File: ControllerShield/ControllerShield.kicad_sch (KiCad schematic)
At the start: 7 parts, among them J1 Power, J2 Digital/PWM, J3 Analog, J4 Digital/PWM, U1 COM-09032, U2 LIS3DH, U3 LSF0102DQER

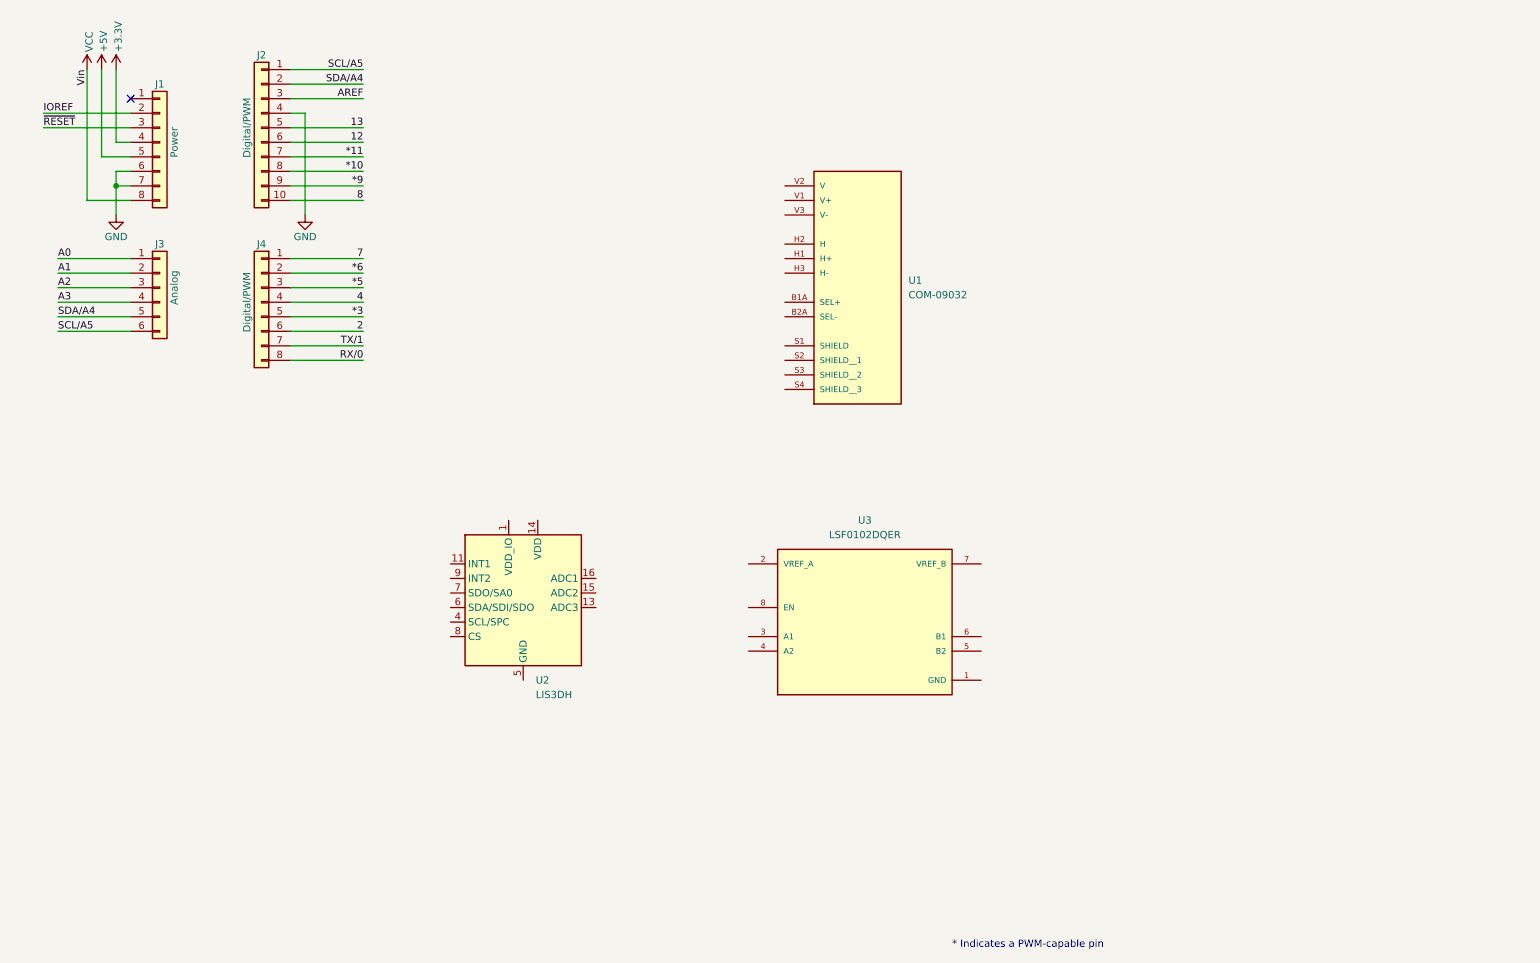
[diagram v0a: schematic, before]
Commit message: Tweak the connector board a bit.  Rearrange X and Y.  May do more depending on the other board.
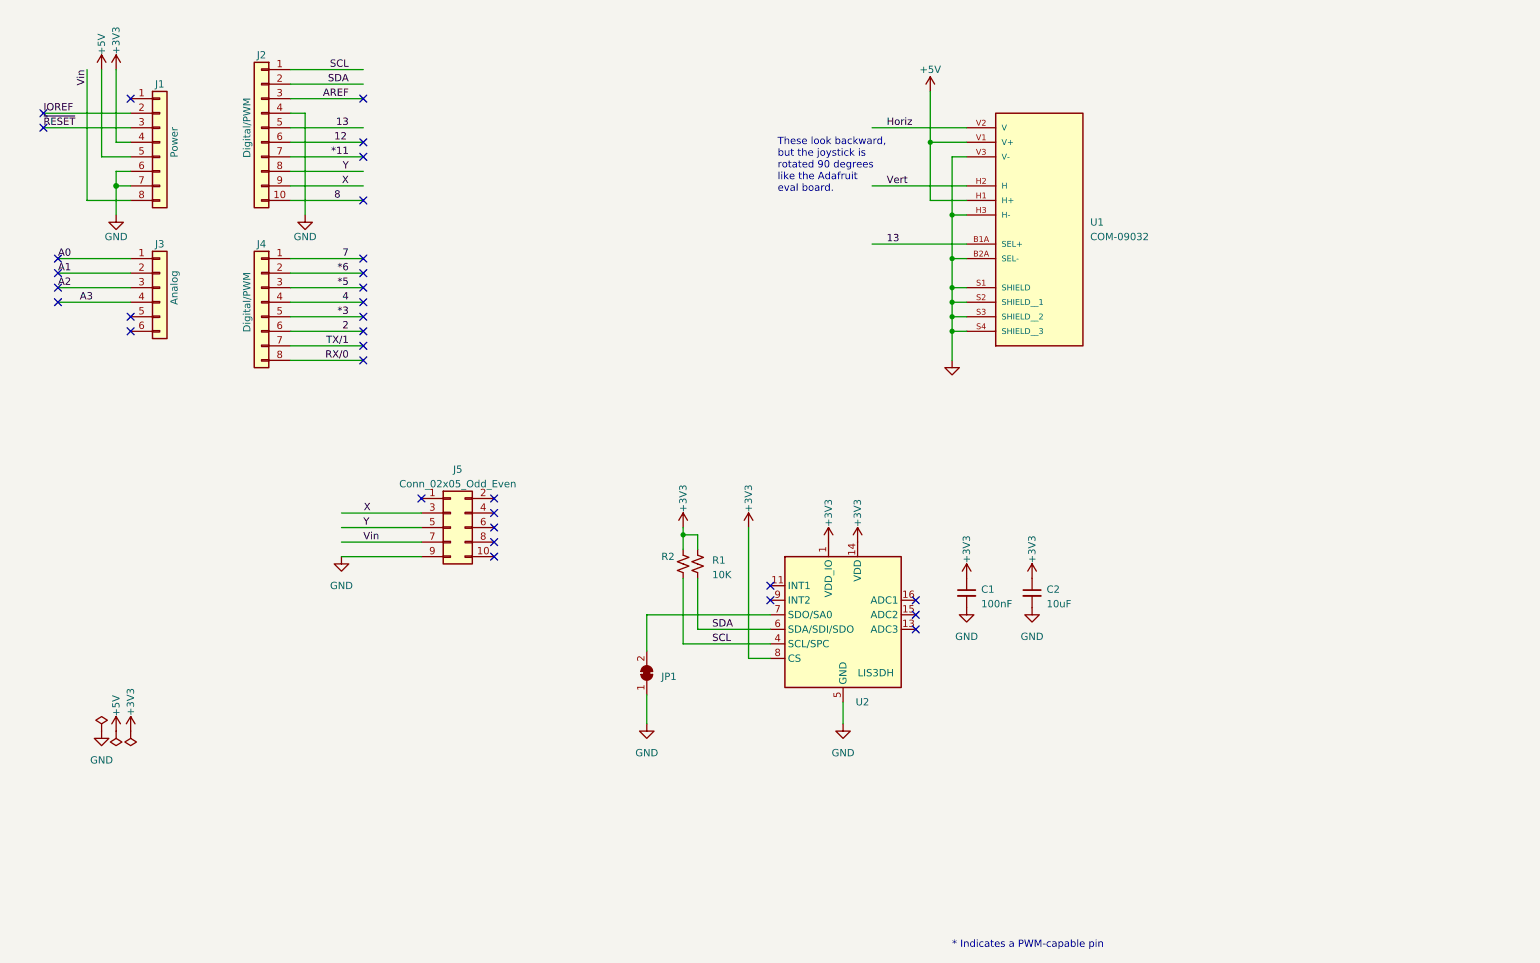
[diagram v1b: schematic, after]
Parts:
- removed U3: LSF0102DQER, Footprints:SON35P140X100X40-8N, symbol Local:LSF0102DQER
- added C1: 100nF, Capacitor_SMD:C_0603_1608Metric, symbol Device:C_Small
- added C2: 10uF, Capacitor_SMD:C_0603_1608Metric, symbol Device:C_Small
- added J5: Conn_02x05_Odd_Even, Connector_PinHeader_2.54mm:PinHeader_2x05_P2.54mm_Vertical, symbol Connector_Generic:Conn_02x05_Odd_Even
- added JP1: SolderJumper_2_Bridged, Jumper:SolderJumper-2_P1.3mm_Bridged_RoundedPad1.0x1.5mm, symbol Jumper:SolderJumper_2_Bridged
- added R1, R2: 10K, Resistor_SMD:R_0603_1608Metric, symbol Device:R_Small_US
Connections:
- net +3V3: now also U2.1 (VDD_IO), U2.14 (VDD), U2.8 (CS), C1.1, C2.1, R1.1, R2.1
- net +5V: now also U1.H1 (H+), U1.V1 (V+)
- net 13: now also U1.B1A (SEL+)
- net GND: now also U1.B2A (SEL-), U1.H3 (H-), U1.S1 (SHIELD), U1.S2 (SHIELD__1), U1.S3 (SHIELD__2), U1.S4 (SHIELD__3), U1.V3 (V-), U2.10 (GND), U2.12 (GND), U2.5 (GND), C1.2, C2.2, J5.9 (Pin_9), JP1.1 (A)
- net Vert: now reaches U1.H2 (H)
- net Horiz: now reaches U1.V2 (V)
- net SCL: now reaches U2.4 (SCL/SPC)
- net SCL: now also J2.1 (Pin_1), R2.2
- net SDA: now reaches U2.6 (SDA/SDI/SDO)
- net SDA: now also J2.2 (Pin_2), R1.2
- net at U2.7 (SDO/SA0): now also JP1.2 (B)
- net *10 renamed Y
- net Y: now also J5.5 (Pin_5)
- net *9 renamed X
- net X: now also J5.3 (Pin_3)
- net SCL/A5: no longer names the net of J3.6 (Pin_6)
- net SCL/A5: no longer J2.1 (Pin_1)
- net SDA/A4: no longer names the net of J3.5 (Pin_5)
- net SDA/A4: no longer J2.2 (Pin_2)
- net VCC renamed Vin
- net Vin: now also J5.7 (Pin_7)
- no-connect marks 1 -> 32
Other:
- note added: "These look backward, but the joystick is rotated 90 degrees like the Adafruit eval board."
- moved on the sheet: U1, U2

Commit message: Not sure what changes, but it was minor...
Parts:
- added D1: RED, symbol Device:LED
- added D2: Green, symbol Device:LED
- added R3, R4: 1K, symbol Device:R_Small_US
- C1: value 100nF -> 0.1uF
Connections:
- net 12 is gone; now on net D1: J2.6 (Pin_6)
- net A0 is gone; now on net Horiz: J3.1 (Pin_1)
- net A1 is gone; now on net Vert: J3.2 (Pin_2)
- net GND: now also D1.1 (K), D2.1 (K)
- net SCL: now also J5.3 (Pin_3)
- net SDA: now also J5.4 (Pin_4)
- net X: now also J5.1 (Pin_1); no longer J5.3 (Pin_3)
- net Y: now also J5.2 (Pin_2); no longer J5.5 (Pin_5)
- net D1: now reaches J5.6 (Pin_6)
- net *3 renamed Red
- net Red: now also R3.1
- net 13 renamed D0
- net D0: now also J5.5 (Pin_5); no longer U1.B1A (SEL+)
- net 2 renamed GameBtn
- net GameBtn: now also U1.B1A (SEL+)
- net 4 renamed Green
- net Green: now also R4.1
- net Vin renamed Vsys
- new net: D2.2 (A), R4.2
- new net: D1.2 (A), R3.2
- no-connect marks 32 -> 22

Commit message: work on controller
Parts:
- D1, D2: footprint (none) -> Diode_THT:D_DO-15_P2.54mm_Vertical_AnodeUp
- R3, R4: footprint (none) -> Resistor_SMD:R_0603_1608Metric
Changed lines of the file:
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@@
       (effects (font (size 1.27 1.27)) (justify left))
     )
-    (property "Footprint" "" (at 116.84 45.72 0)
+    (property "Footprint" "Resistor_SMD:R_0603_1608Metric" (at 116.84 45.72 0)
       (effects (font (size 1.27 1.27)) hide)
     )
@@
       (effects (font (size 1.27 1.27)) (justify right))
     )
-    (property "Footprint" "" (at 116.84 54.61 0)
+    (property "Footprint" "Diode_THT:D_DO-15_P2.54mm_Vertical_AnodeUp" (at 116.84 54.61 0)
       (effects (font (size 1.27 1.27)) hide)
     )
@@
       (effects (font (size 1.27 1.27)) (justify right))
     )
-    (property "Footprint" "" (at 109.22 54.61 0)
+    (property "Footprint" "Diode_THT:D_DO-15_P2.54mm_Vertical_AnodeUp" (at 109.22 54.61 0)
       (effects (font (size 1.27 1.27)) hide)
     )
@@
       (effects (font (size 1.27 1.27)) (justify left))
     )
-    (property "Footprint" "" (at 109.22 45.72 0)
-      (effects (font (size 1.27 1.27)) hide)
-    )
+    (property "Footprint" "Resistor_SMD:R_0603_1608Metric" (at 109.22 45.72 0)
+      (effects (font (size 1.27 1.27)) hide)
+    )

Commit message: work on controller
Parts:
- added U3: TLV75533PDBV, Package_TO_SOT_SMD:SOT-23-5, symbol Regulator_Linear:TLV75533PDBV
- D1, D2: footprint Diode_THT:D_DO-15_P2.54mm_Vertical_AnodeUp -> LED_THT:LED_D5.0mm
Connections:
- net +3V3: now also U3.5 (OUT); no longer J1.4 (Pin_4)
- net +5V: now also U3.1 (IN), U3.3 (EN)
- net GND: now also U3.2 (GND)
- no-connect marks 22 -> 23
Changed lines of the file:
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@@
   (junction (at 177.8 52.07) (diameter 0) (color 0 0 0 0)
+  )
+  (junction (at 118.11 76.2) (diameter 0) (color 0 0 0 0)
   )
   (junction (at 177.8 72.39) (diameter 0) (color 0 0 0 0)
@@
   (no_connect (at 74.93 62.23))
   (no_connect (at 74.93 77.47))
+  (no_connect (at 34.29 39.37))
   (no_connect (at 74.93 31.75))
   (wire (pts (xy 62.23 77.47) (xy 74.93 77.47))
@@
     (stroke (width 0) (type default))
   )
-  (wire (pts (xy 31.75 39.37) (xy 34.29 39.37))
-    (stroke (width 0) (type solid))
-  )
   (wire (pts (xy 29.21 41.91) (xy 34.29 41.91))
     (stroke (width 0) (type solid))
@@
     (stroke (width 0) (type default))
   )
-  (wire (pts (xy 31.75 26.67) (xy 31.75 39.37))
-    (stroke (width 0) (type solid))
-  )
   (wire (pts (xy 62.23 59.69) (xy 74.93 59.69))
     (stroke (width 0) (type solid))
@@
     (stroke (width 0) (type solid))
   )
+  (wire (pts (xy 109.22 76.2) (xy 118.11 76.2))
+    (stroke (width 0) (type default))
+  )
   (wire (pts (xy 177.8 72.39) (xy 180.34 72.39))
     (stroke (width 0) (type default))
   )
+  (wire (pts (xy 119.38 78.74) (xy 118.11 78.74))
+    (stroke (width 0) (type default))
+  )
   (wire (pts (xy 180.34 41.91) (xy 177.8 41.91))
     (stroke (width 0) (type default))
@@
     (stroke (width 0) (type default))
   )
+  (wire (pts (xy 134.62 76.2) (xy 144.78 76.2))
+    (stroke (width 0) (type default))
+  )
   (wire (pts (xy 34.29 49.53) (xy 26.67 49.53))
     (stroke (width 0) (type solid))
   )
+  (wire (pts (xy 118.11 76.2) (xy 119.38 76.2))
+    (stroke (width 0) (type default))
+  )
   (wire (pts (xy 21.59 62.23) (xy 34.29 62.23))
     (stroke (width 0) (type solid))
   )
   (wire (pts (xy 85.09 109.22) (xy 71.12 109.22))
+    (stroke (width 0) (type default))
+  )
+  (wire (pts (xy 118.11 78.74) (xy 118.11 76.2))
     (stroke (width 0) (type default))
   )
@@
     )
   )
-  (symbol (lib_id "power:PWR_FLAG") (at 34.29 142.24 180) (unit 1)
-    (in_bom yes) (on_board yes) (dnp no) (fields_autoplaced)
-    (property "Reference" "#FLG03" (at 34.29 144.145 0)
-      (effects (font (size 1.27 1.27)) hide)
-    )
-    (property "Value" "PWR_FLAG" (at 34.29 146.05 0)
-      (effects (font (size 1.27 1.27)) hide)
-    )
-    (property "Footprint" "" (at 34.29 142.24 0)
-      (effects (font (size 1.27 1.27)) hide)
-    )
-    (property "Datasheet" "~" (at 34.29 142.24 0)
-      (effects (font (size 1.27 1.27)) hide)
-    )
-    (pin "1")
-    (instances
-      (project "ControllerShield"
-        (path "/e63e39d7-6ac0-4ffd-8aa3-1841a4541b55"
-          (reference "#FLG03") (unit 1)
-        )
-      )
-    )
-  )
   (symbol (lib_id "Connector_Generic:Conn_02x05_Odd_Even") (at 90.17 106.68 0) (unit 1)
     (in_bom yes) (on_board yes) (dnp no) (fields_autoplaced)
@@
       (effects (font (size 1.27 1.27)) (justify right))
     )
-    (property "Footprint" "Diode_THT:D_DO-15_P2.54mm_Vertical_AnodeUp" (at 116.84 54.61 0)
+    (property "Footprint" "LED_THT:LED_D5.0mm" (at 116.84 54.61 0)
       (effects (font (size 1.27 1.27)) hide)
     )
@@
     )
   )
-  (symbol (lib_id "power:+3V3") (at 34.29 142.24 0) (unit 1)
-    (in_bom yes) (on_board yes) (dnp no)
-    (property "Reference" "#PWR011" (at 34.29 146.05 0)
-      (effects (font (size 1.27 1.27)) hide)
-    )
-    (property "Value" "+3V3" (at 34.29 137.16 90)
-      (effects (font (size 1.27 1.27)))
-    )
-    (property "Footprint" "" (at 34.29 142.24 0)
-      (effects (font (size 1.27 1.27)) hide)
-    )
-    (property "Datasheet" "" (at 34.29 142.24 0)
-      (effects (font (size 1.27 1.27)) hide)
-    )
-    (pin "1")
-    (instances
-      (project "ControllerShield"
-        (path "/e63e39d7-6ac0-4ffd-8aa3-1841a4541b55"
-          (reference "#PWR011") (unit 1)
+  (symbol (lib_id "Regulator_Linear:TLV75533PDBV") (at 127 78.74 0) (unit 1)
+    (in_bom yes) (on_board yes) (dnp no) (fields_autoplaced)
+    (property "Reference" "U3" (at 127 69.85 0)
+      (effects (font (size 1.27 1.27)))
+    )
+    (property "Value" "TLV75533PDBV" (at 127 72.39 0)
+      (effects (font (size 1.27 1.27)))
+    )
+    (property "Footprint" "Package_TO_SOT_SMD:SOT-23-5" (at 127 70.485 0)
+      (effects (font (size 1.27 1.27) italic) hide)
+    )
+    (property "Datasheet" "http://www.ti.com/lit/ds/symlink/tlv755p.pdf" (at 127 77.47 0)
+      (effects (font (size 1.27 1.27)) hide)
+    )
+    (pin "1")
+    (pin "2")
+    (pin "3")
+    (pin "4")
+    (pin "5")
+    (instances
+      (project "ControllerShield"
+        (path "/e63e39d7-6ac0-4ffd-8aa3-1841a4541b55"
+          (reference "U3") (unit 1)
         )
       )
@@
     )
   )
-  (symbol (lib_id "power:+3V3") (at 31.75 26.67 0) (unit 1)
-    (in_bom yes) (on_board yes) (dnp no)
-    (property "Reference" "#PWR03" (at 31.75 30.48 0)
-      (effects (font (size 1.27 1.27)) hide)
-    )
-    (property "Value" "+3V3" (at 31.75 21.59 90)
-      (effects (font (size 1.27 1.27)))
-    )
-    (property "Footprint" "" (at 31.75 26.67 0)
-      (effects (font (size 1.27 1.27)) hide)
-    )
-    (property "Datasheet" "" (at 31.75 26.67 0)
-      (effects (font (size 1.27 1.27)) hide)
-    )
-    (pin "1")
-    (instances
-      (project "ControllerShield"
-        (path "/e63e39d7-6ac0-4ffd-8aa3-1841a4541b55"
-          (reference "#PWR03") (unit 1)
-        )
-      )
-    )
-  )
   (symbol (lib_id "power:PWR_FLAG") (at 29.21 142.24 0) (unit 1)
     (in_bom yes) (on_board yes) (dnp no) (fields_autoplaced)
@@
         (path "/e63e39d7-6ac0-4ffd-8aa3-1841a4541b55"
           (reference "#PWR06") (unit 1)
+        )
+      )
+    )
+  )
+  (symbol (lib_id "power:+5V") (at 109.22 76.2 0) (unit 1)
+    (in_bom yes) (on_board yes) (dnp no) (fields_autoplaced)
+    (property "Reference" "#PWR023" (at 109.22 80.01 0)
+      (effects (font (size 1.27 1.27)) hide)
+    )
+    (property "Value" "+5V" (at 109.22 71.12 0)
+      (effects (font (size 1.27 1.27)))
+    )
+    (property "Footprint" "" (at 109.22 76.2 0)
+      (effects (font (size 1.27 1.27)) hide)
+    )
+    (property "Datasheet" "" (at 109.22 76.2 0)
+      (effects (font (size 1.27 1.27)) hide)
+    )
+    (pin "1")
+    (instances
+      (project "ControllerShield"
+        (path "/e63e39d7-6ac0-4ffd-8aa3-1841a4541b55"
+          (reference "#PWR023") (unit 1)
+        )
+      )
+    )
+  )
+  (symbol (lib_id "power:+3V3") (at 144.78 76.2 0) (unit 1)
+    (in_bom yes) (on_board yes) (dnp no)
+    (property "Reference" "#PWR024" (at 144.78 80.01 0)
+      (effects (font (size 1.27 1.27)) hide)
+    )
+    (property "Value" "+3V3" (at 144.78 71.12 90)
+      (effects (font (size 1.27 1.27)))
+    )
+    (property "Footprint" "" (at 144.78 76.2 0)
+      (effects (font (size 1.27 1.27)) hide)
+    )
+    (property "Datasheet" "" (at 144.78 76.2 0)
+      (effects (font (size 1.27 1.27)) hide)
+    )
+    (pin "1")
+    (instances
+      (project "ControllerShield"
+        (path "/e63e39d7-6ac0-4ffd-8aa3-1841a4541b55"
+          (reference "#PWR024") (unit 1)
         )
       )
@@
       (effects (font (size 1.27 1.27)) (justify right))
     )
-    (property "Footprint" "Diode_THT:D_DO-15_P2.54mm_Vertical_AnodeUp" (at 109.22 54.61 0)
+    (property "Footprint" "LED_THT:LED_D5.0mm" (at 109.22 54.61 0)
       (effects (font (size 1.27 1.27)) hide)
     )
@@
         )
       )
+    )
+  )
+  (symbol (lib_id "power:GND") (at 127 86.36 0) (unit 1)
+    (in_bom yes) (on_board yes) (dnp no) (fields_autoplaced)
+    (property "Reference" "#PWR03" (at 127 92.71 0)
+      (effects (font (size 1.27 1.27)) hide)
+    )
+    (property "Value" "GND" (at 127 91.44 0)
+      (effects (font (size 1.27 1.27)) hide)
+    )
+    (property "Footprint" "" (at 127 86.36 0)
+      (effects (font (size 1.27 1.27)) hide)
+    )
+    (property "Datasheet" "" (at 127 86.36 0)
+      (effects (font (size 1.27 1.27)) hide)
+    )
+    (pin "1")
+    (instances
+      (project "ControllerShield"
+        (path "/e63e39d7-6ac0-4ffd-8aa3-1841a4541b55"
+          (reference "#PWR03") (unit 1)
+        )
+      )
